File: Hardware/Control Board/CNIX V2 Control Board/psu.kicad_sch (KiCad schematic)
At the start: 37 parts, among them Q100 MMBTA42, Q101 FDS2734, U100 UCC3803

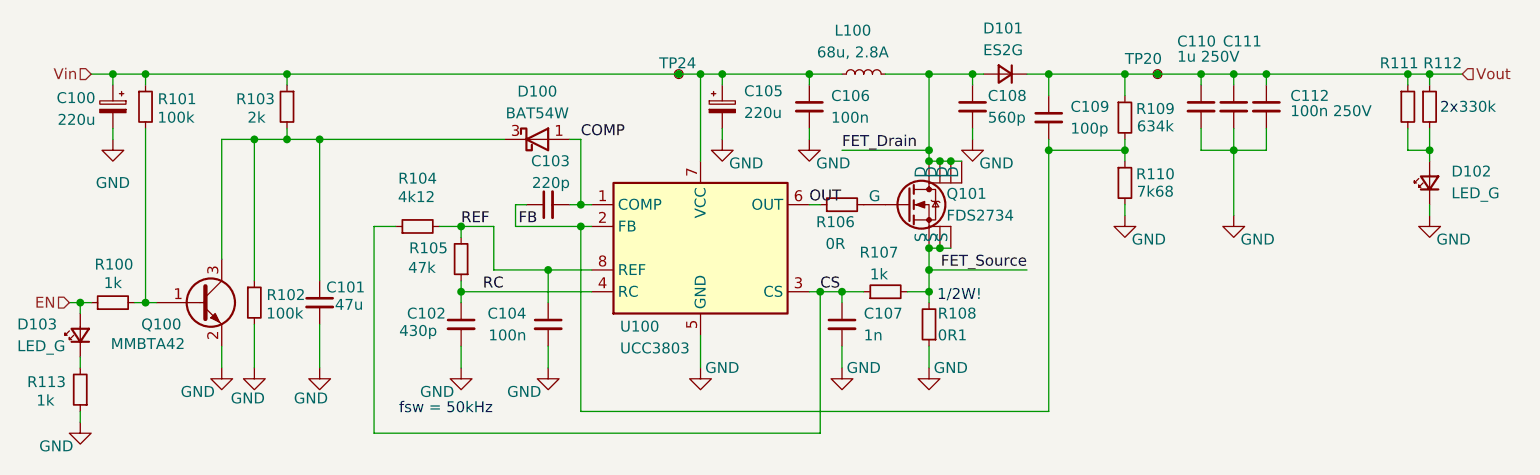
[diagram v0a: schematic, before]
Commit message: added bom and mouser nr
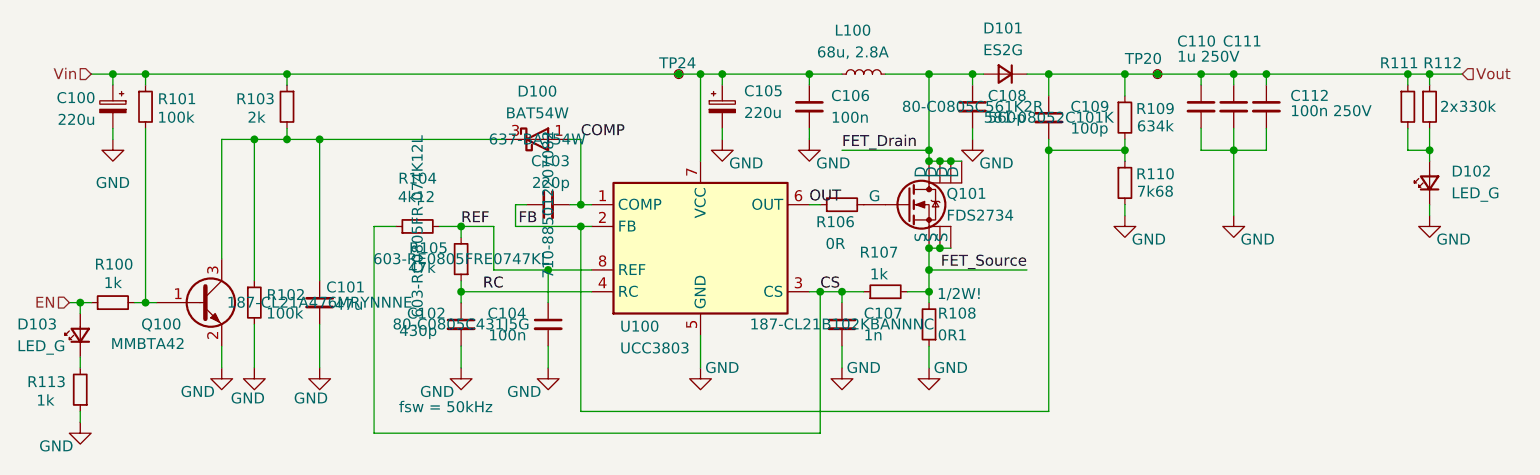
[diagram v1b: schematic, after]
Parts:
- C100, C105: Mouser Nr. (none) -> 647-UUX1E221MNL6GS
- C101: Mouser Nr. (none) -> 187-CL21A476MRYNNNE
- C102: Mouser Nr. (none) -> 80-C0805C431J5G
- C103: Mouser Nr. (none) -> 710-885012207082
- C107: Mouser Nr. (none) -> 187-CL21B102KBANNNC
- C108: Mouser Nr. (none) -> 80-C0805C561K2R
- C109: Mouser Nr. (none) -> 581-08052C101K
- C110, C111, C112: Mouser Nr. (none) -> 810-CGA4J3X7T2E104MA
- D100: Mouser Nr. (none) -> 637-BAT54W; Mouser-Nr. (none) -> 637-BAT54W
- R103: Mouser Nr. (none) -> 603-RC0805FR-132KL
- R104: Mouser Nr. (none) -> 603-RC0805FR-074K12L
- R105: Mouser Nr. (none) -> 603-RE0805FRE0747KL
- R109: Mouser Nr. (none) -> 71-CRCW0805634KFKEA
- R110: Mouser Nr. (none) -> 603-RC0805FR-077K68L
- R111, R112: Mouser Nr. (none) -> 603-AC0805FR-07330KL
- U100: Mouser Nr. (none) -> 595-UCC3803DTR
